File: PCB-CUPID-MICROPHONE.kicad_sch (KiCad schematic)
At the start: 6 parts, among them J2 Conn_01x05

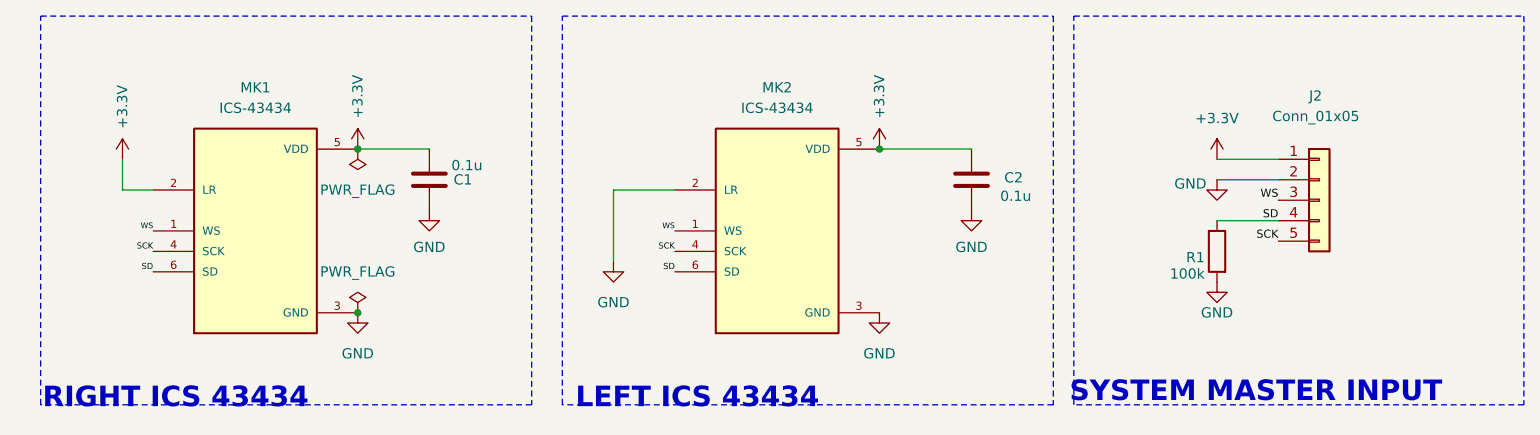
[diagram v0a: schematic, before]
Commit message: updated pcbcupid-mic-2ch files
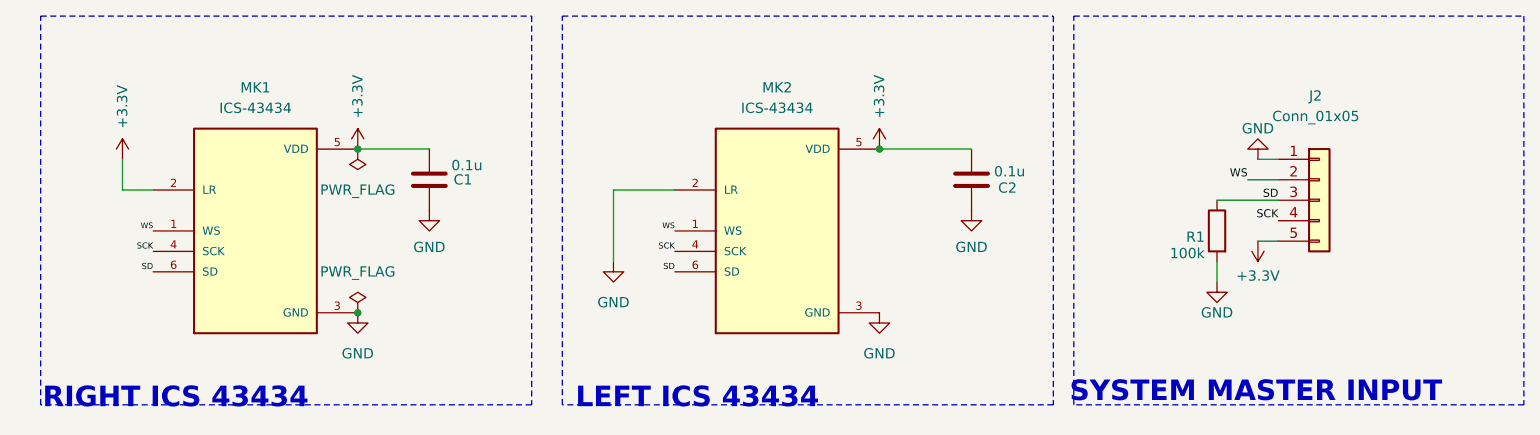
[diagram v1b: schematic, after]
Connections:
- net +3.3V: now also J2.5 (Pin_5); no longer J2.1 (Pin_1)
- net GND: now also J2.1 (Pin_1); no longer J2.2 (Pin_2)
- net SCK: now also J2.4 (Pin_4); no longer J2.5 (Pin_5)
- net SD: now also J2.3 (Pin_3); no longer J2.4 (Pin_4)
- net WS: now also J2.2 (Pin_2); no longer J2.3 (Pin_3)
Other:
- moved on the sheet: R1
